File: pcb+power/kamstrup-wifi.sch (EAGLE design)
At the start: 26 parts, among them T1 BT137, T2 BT137, U1 ESP8266-07, U2 MCP1316T-29LE/OT

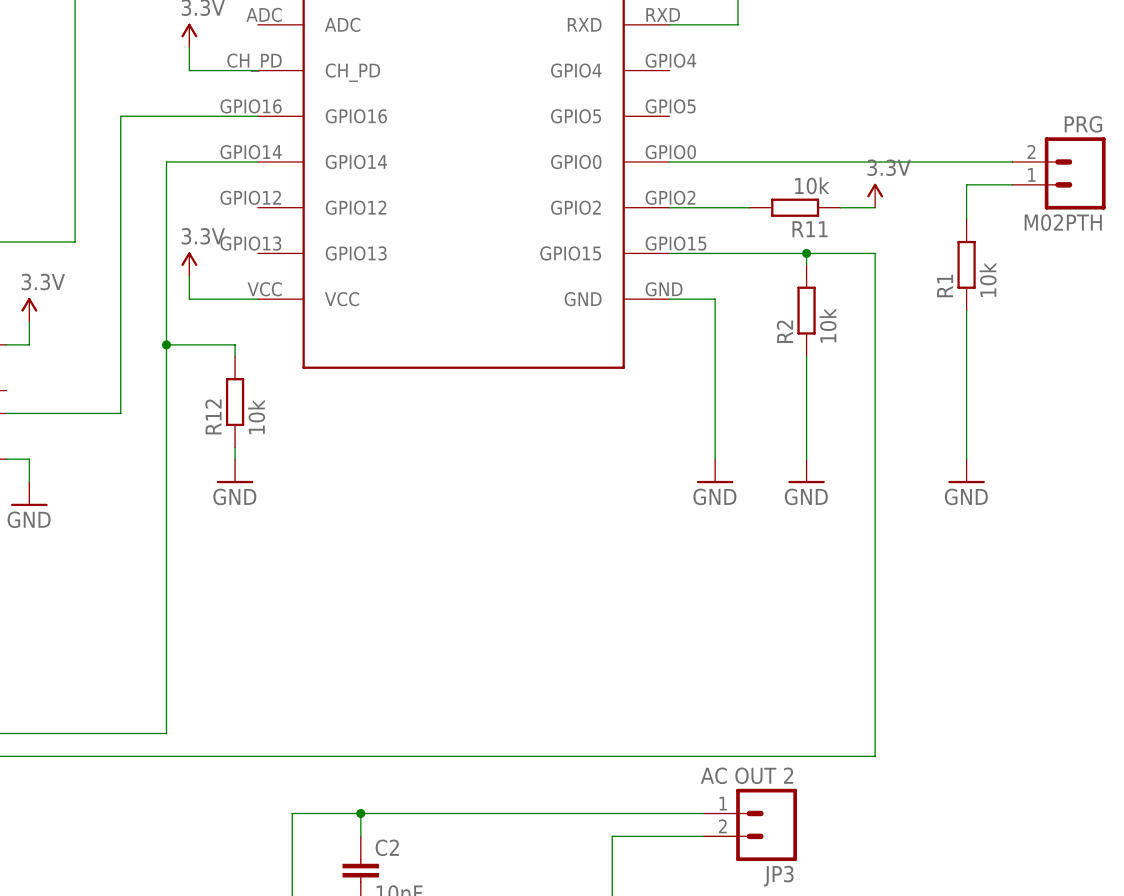
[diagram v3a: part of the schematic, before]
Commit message: reverted pcb to v 1.2.1 2377baf1af9bc101ab4e1265beb616f56084d54c no pull down needed
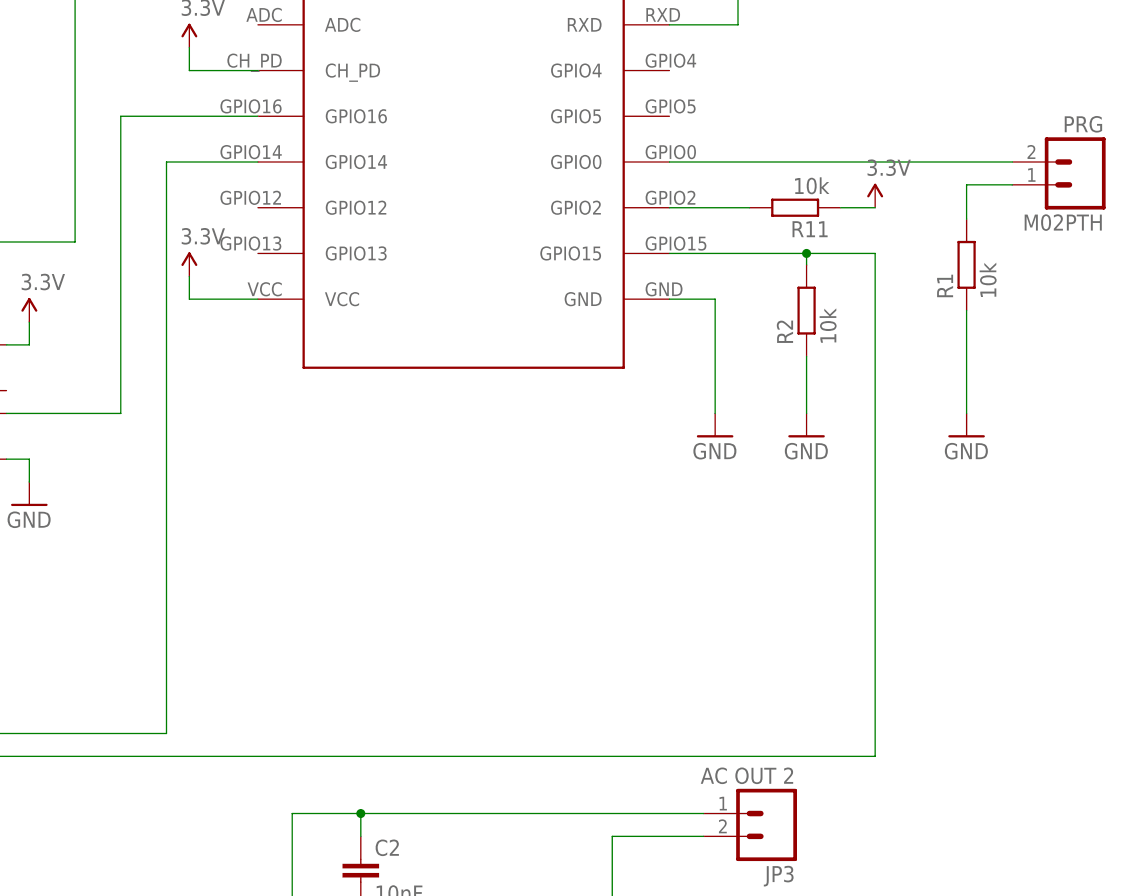
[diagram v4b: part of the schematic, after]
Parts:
- removed R12: 10k, rcl:R-EU_R0805
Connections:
- net GND: no longer R12.1
- net N$11: no longer R12.2
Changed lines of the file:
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@@
 <?xml version="1.0" encoding="utf-8"?>
 <!DOCTYPE eagle SYSTEM "eagle.dtd">
-<eagle version="8.1.1">
+<eagle version="7.6.0">
 <drawing>
 <settings>
@@
 <setting verticaltext="up"/>
 </settings>
-<grid distance="0.1" unitdist="inch" unit="inch" style="lines" multiple="1" display="no" altdistance="0.01" altunitdist="inch" altunit="inch"/>
+<grid distance="0.05" unitdist="inch" unit="inch" style="lines" multiple="1" display="no" altdistance="0.005" altunitdist="inch" altunit="inch"/>
 <layers>
 <layer number="1" name="Top" color="4" fill="1" visible="no" active="no"/>
@@
 <part name="SUPPLY5" library="SparkFun-Aesthetics" deviceset="3.3V" device=""/>
 <part name="R11" library="rcl" deviceset="R-EU_" device="R0805" value="10k"/>
-<part name="R12" library="rcl" deviceset="R-EU_" device="R0805" value="10k"/>
-<part name="GND9" library="SparkFun-Aesthetics" deviceset="GND" device=""/>
 </parts>
 <sheets>
@@
 <attribute name="NAME" x="180.34" y="61.722" size="1.778" layer="95" rot="MR0"/>
 </instance>
-<instance part="GND5" gate="1" x="165.1" y="22.86"/>
+<instance part="GND5" gate="1" x="165.1" y="27.94"/>
 <instance part="R1" gate="G$1" x="165.1" y="46.99" rot="R90"/>
 <instance part="OK2" gate="-1" x="46.99" y="-31.75"/>
@@
 <instance part="T2" gate="G$1" x="80.01" y="-31.75"/>
 <instance part="U1" gate="G$1" x="106.68" y="53.34"/>
-<instance part="GND8" gate="1" x="137.16" y="22.86"/>
+<instance part="GND8" gate="1" x="137.16" y="27.94"/>
 <instance part="SUPPLY2" gate="G$1" x="78.74" y="71.12"/>
 <instance part="SUPPLY7" gate="G$1" x="78.74" y="45.72"/>
 <instance part="U2" gate="A" x="40.64" y="35.56" rot="MR0"/>
 <instance part="R2" gate="G$1" x="147.32" y="41.91" rot="R90"/>
-<instance part="GND3" gate="1" x="147.32" y="22.86"/>
+<instance part="GND3" gate="1" x="147.32" y="27.94"/>
 <instance part="SUPPLY3" gate="G$1" x="60.96" y="40.64"/>
 <instance part="GND7" gate="1" x="60.96" y="20.32"/>
 <instance part="SUPPLY5" gate="G$1" x="154.94" y="53.34"/>
 <instance part="R11" gate="G$1" x="146.05" y="53.34" rot="R180"/>
-<instance part="R12" gate="G$1" x="83.82" y="31.75" rot="R90"/>
-<instance part="GND9" gate="1" x="83.82" y="22.86"/>
 </instances>
 <busses>
@@
 <pinref part="GND5" gate="1" pin="GND"/>
 <pinref part="R1" gate="G$1" pin="1"/>
-<wire x1="165.1" y1="25.4" x2="165.1" y2="41.91" width="0.1524" layer="91"/>
+<wire x1="165.1" y1="30.48" x2="165.1" y2="41.91" width="0.1524" layer="91"/>
 </segment>
 <segment>
@@
 <pinref part="GND8" gate="1" pin="GND"/>
 <wire x1="132.08" y1="43.18" x2="137.16" y2="43.18" width="0.1524" layer="91"/>
-<wire x1="137.16" y1="43.18" x2="137.16" y2="25.4" width="0.1524" layer="91"/>
+<wire x1="137.16" y1="43.18" x2="137.16" y2="30.48" width="0.1524" layer="91"/>
 </segment>
 <segment>
 <pinref part="GND3" gate="1" pin="GND"/>
 <pinref part="R2" gate="G$1" pin="1"/>
-<wire x1="147.32" y1="25.4" x2="147.32" y2="36.83" width="0.1524" layer="91"/>
+<wire x1="147.32" y1="30.48" x2="147.32" y2="36.83" width="0.1524" layer="91"/>
 </segment>
 <segment>
@@
 <wire x1="58.42" y1="25.4" x2="60.96" y2="25.4" width="0.1524" layer="91"/>
 <wire x1="60.96" y1="25.4" x2="60.96" y2="22.86" width="0.1524" layer="91"/>
-</segment>
-<segment>
-<pinref part="GND9" gate="1" pin="GND"/>
-<pinref part="R12" gate="G$1" pin="1"/>
-<wire x1="83.82" y1="25.4" x2="83.82" y2="26.67" width="0.1524" layer="91"/>
 </segment>
 </net>
@@
 <net name="N$11" class="0">
 <segment>
-<wire x1="76.2" y1="-5.08" x2="76.2" y2="38.1" width="0.1524" layer="91"/>
+<wire x1="76.2" y1="-5.08" x2="76.2" y2="58.42" width="0.1524" layer="91"/>
 <pinref part="U1" gate="G$1" pin="GPIO14"/>
-<wire x1="76.2" y1="38.1" x2="76.2" y2="58.42" width="0.1524" layer="91"/>
 <wire x1="76.2" y1="58.42" x2="86.36" y2="58.42" width="0.1524" layer="91"/>
 <wire x1="76.2" y1="-5.08" x2="8.89" y2="-5.08" width="0.1524" layer="91"/>
@@
 <pinref part="R3" gate="G$1" pin="1"/>
 <wire x1="8.89" y1="-67.31" x2="19.05" y2="-67.31" width="0.1524" layer="91"/>
-<pinref part="R12" gate="G$1" pin="2"/>
-<wire x1="83.82" y1="36.83" x2="83.82" y2="38.1" width="0.1524" layer="91"/>
-<wire x1="83.82" y1="38.1" x2="76.2" y2="38.1" width="0.1524" layer="91"/>
-<junction x="76.2" y="38.1"/>
-</segment>
-</net>
+</segment>
+</net>

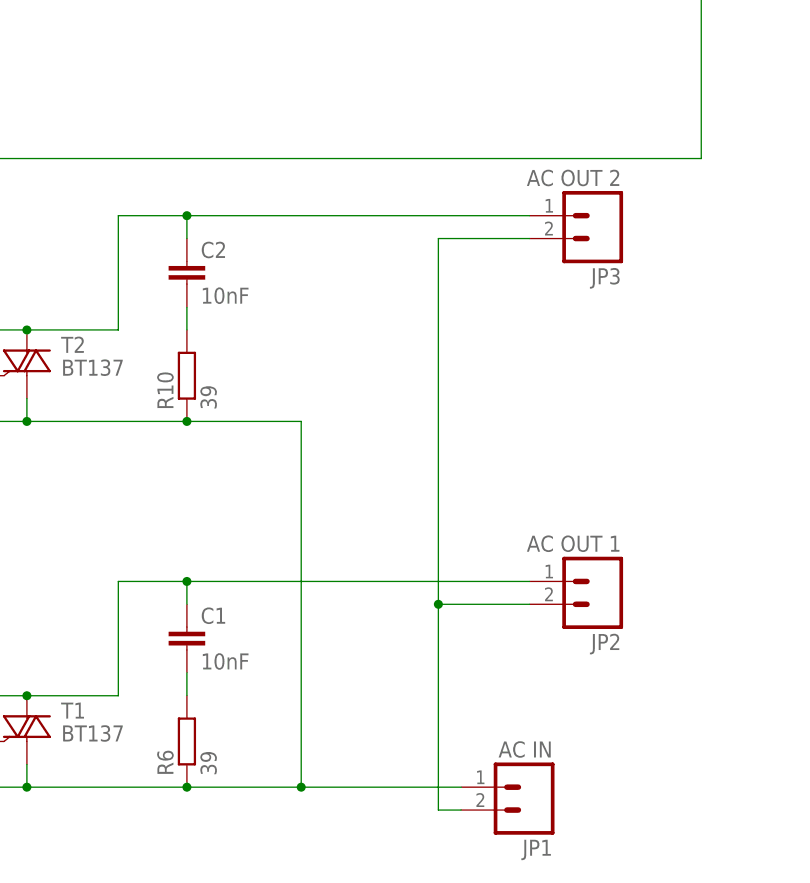
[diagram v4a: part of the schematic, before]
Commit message: Labels for N and L on AC in/out
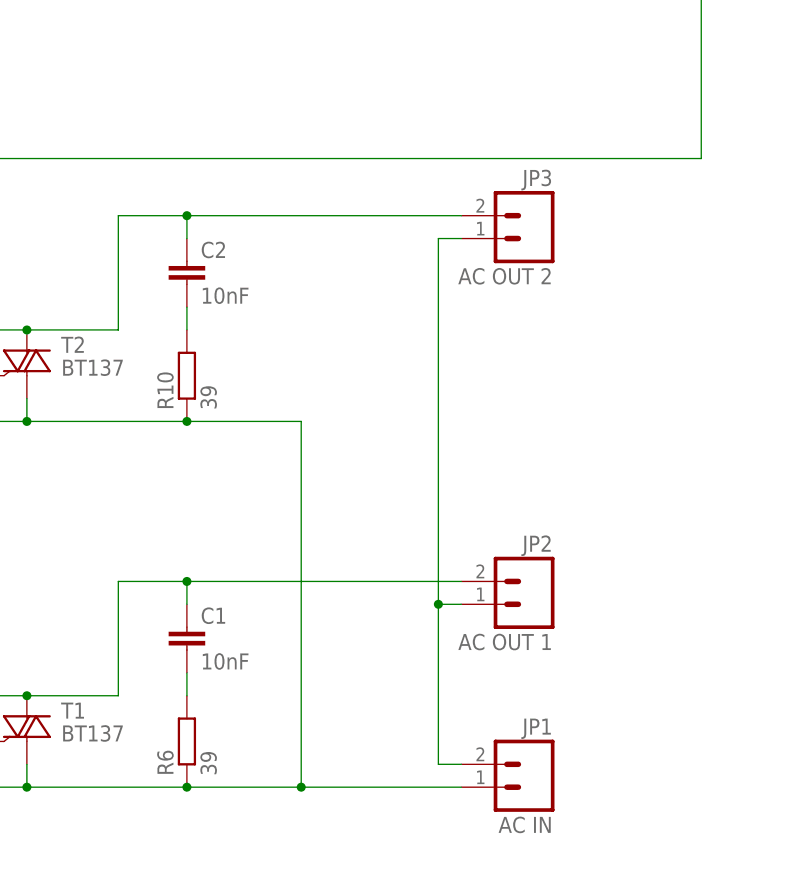
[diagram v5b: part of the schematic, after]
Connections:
- net N$15: now also JP2.2; no longer JP2.1
- net N$18: now also JP2.1, JP3.1; no longer JP2.2, JP3.2
- net N$8: now also JP3.2; no longer JP3.1
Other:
- moved on the sheet: JP1, JP2, JP3
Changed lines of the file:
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@@
 <?xml version="1.0" encoding="utf-8"?>
 <!DOCTYPE eagle SYSTEM "eagle.dtd">
-<eagle version="7.6.0">
+<eagle version="8.2.1">
 <drawing>
 <settings>
@@
 <instance part="R10" gate="G$1" x="97.79" y="-31.75" rot="R90"/>
 <instance part="C2" gate="G$1" x="97.79" y="-19.05"/>
-<instance part="JP3" gate="G$1" x="143.51" y="-13.97" rot="R180"/>
+<instance part="JP3" gate="G$1" x="135.89" y="-16.51" rot="MR0"/>
 <instance part="OK1" gate="-1" x="46.99" y="-72.39"/>
 <instance part="GND2" gate="1" x="31.75" y="-82.55"/>
@@
 <instance part="R6" gate="G$1" x="97.79" y="-72.39" rot="R90"/>
 <instance part="C1" gate="G$1" x="97.79" y="-59.69"/>
-<instance part="JP1" gate="G$1" x="135.89" y="-77.47" rot="R180"/>
-<instance part="JP2" gate="G$1" x="143.51" y="-54.61" rot="R180"/>
+<instance part="JP1" gate="G$1" x="135.89" y="-77.47" rot="MR0"/>
+<instance part="JP2" gate="G$1" x="135.89" y="-57.15" rot="MR0"/>
 <instance part="T1" gate="G$1" x="80.01" y="-72.39"/>
 <instance part="T2" gate="G$1" x="80.01" y="-31.75"/>
@@
 <wire x1="90.17" y1="-13.97" x2="97.79" y2="-13.97" width="0.1524" layer="91"/>
 <pinref part="C2" gate="G$1" pin="1"/>
-<wire x1="97.79" y1="-13.97" x2="135.89" y2="-13.97" width="0.1524" layer="91"/>
 <wire x1="97.79" y1="-16.51" x2="97.79" y2="-13.97" width="0.1524" layer="91"/>
-<junction x="97.79" y="-13.97"/>
-<pinref part="JP3" gate="G$1" pin="1"/>
 <pinref part="T2" gate="G$1" pin="A2"/>
 <junction x="80.01" y="-26.67"/>
+<pinref part="JP3" gate="G$1" pin="2"/>
+<wire x1="128.27" y1="-13.97" x2="97.79" y2="-13.97" width="0.1524" layer="91"/>
+<junction x="97.79" y="-13.97"/>
 </segment>
 </net>
@@
 <wire x1="90.17" y1="-54.61" x2="97.79" y2="-54.61" width="0.1524" layer="91"/>
 <pinref part="C1" gate="G$1" pin="1"/>
-<wire x1="97.79" y1="-54.61" x2="135.89" y2="-54.61" width="0.1524" layer="91"/>
 <wire x1="97.79" y1="-57.15" x2="97.79" y2="-54.61" width="0.1524" layer="91"/>
-<junction x="97.79" y="-54.61"/>
-<pinref part="JP2" gate="G$1" pin="1"/>
 <pinref part="T1" gate="G$1" pin="A2"/>
 <junction x="80.01" y="-67.31"/>
+<pinref part="JP2" gate="G$1" pin="2"/>
+<wire x1="128.27" y1="-54.61" x2="97.79" y2="-54.61" width="0.1524" layer="91"/>
+<junction x="97.79" y="-54.61"/>
 </segment>
 </net>
@@
 <net name="N$18" class="0">
 <segment>
-<pinref part="JP2" gate="G$1" pin="2"/>
-<wire x1="135.89" y1="-57.15" x2="125.73" y2="-57.15" width="0.1524" layer="91"/>
+<wire x1="125.73" y1="-74.93" x2="125.73" y2="-57.15" width="0.1524" layer="91"/>
 <wire x1="125.73" y1="-57.15" x2="125.73" y2="-16.51" width="0.1524" layer="91"/>
-<pinref part="JP3" gate="G$1" pin="2"/>
-<wire x1="125.73" y1="-16.51" x2="135.89" y2="-16.51" width="0.1524" layer="91"/>
 <pinref part="JP1" gate="G$1" pin="2"/>
-<wire x1="128.27" y1="-80.01" x2="125.73" y2="-80.01" width="0.1524" layer="91"/>
-<wire x1="125.73" y1="-80.01" x2="125.73" y2="-57.15" width="0.1524" layer="91"/>
+<wire x1="128.27" y1="-74.93" x2="125.73" y2="-74.93" width="0.1524" layer="91"/>
+<pinref part="JP2" gate="G$1" pin="1"/>
+<wire x1="128.27" y1="-57.15" x2="125.73" y2="-57.15" width="0.1524" layer="91"/>
 <junction x="125.73" y="-57.15"/>
-</segment>
-</net>
+<pinref part="JP3" gate="G$1" pin="1"/>
+<wire x1="128.27" y1="-16.51" x2="125.73" y2="-16.51" width="0.1524" layer="91"/>
+</segment>
+</net>
